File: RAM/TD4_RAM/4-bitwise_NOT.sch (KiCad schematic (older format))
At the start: 2 parts, among them U3 74HC04

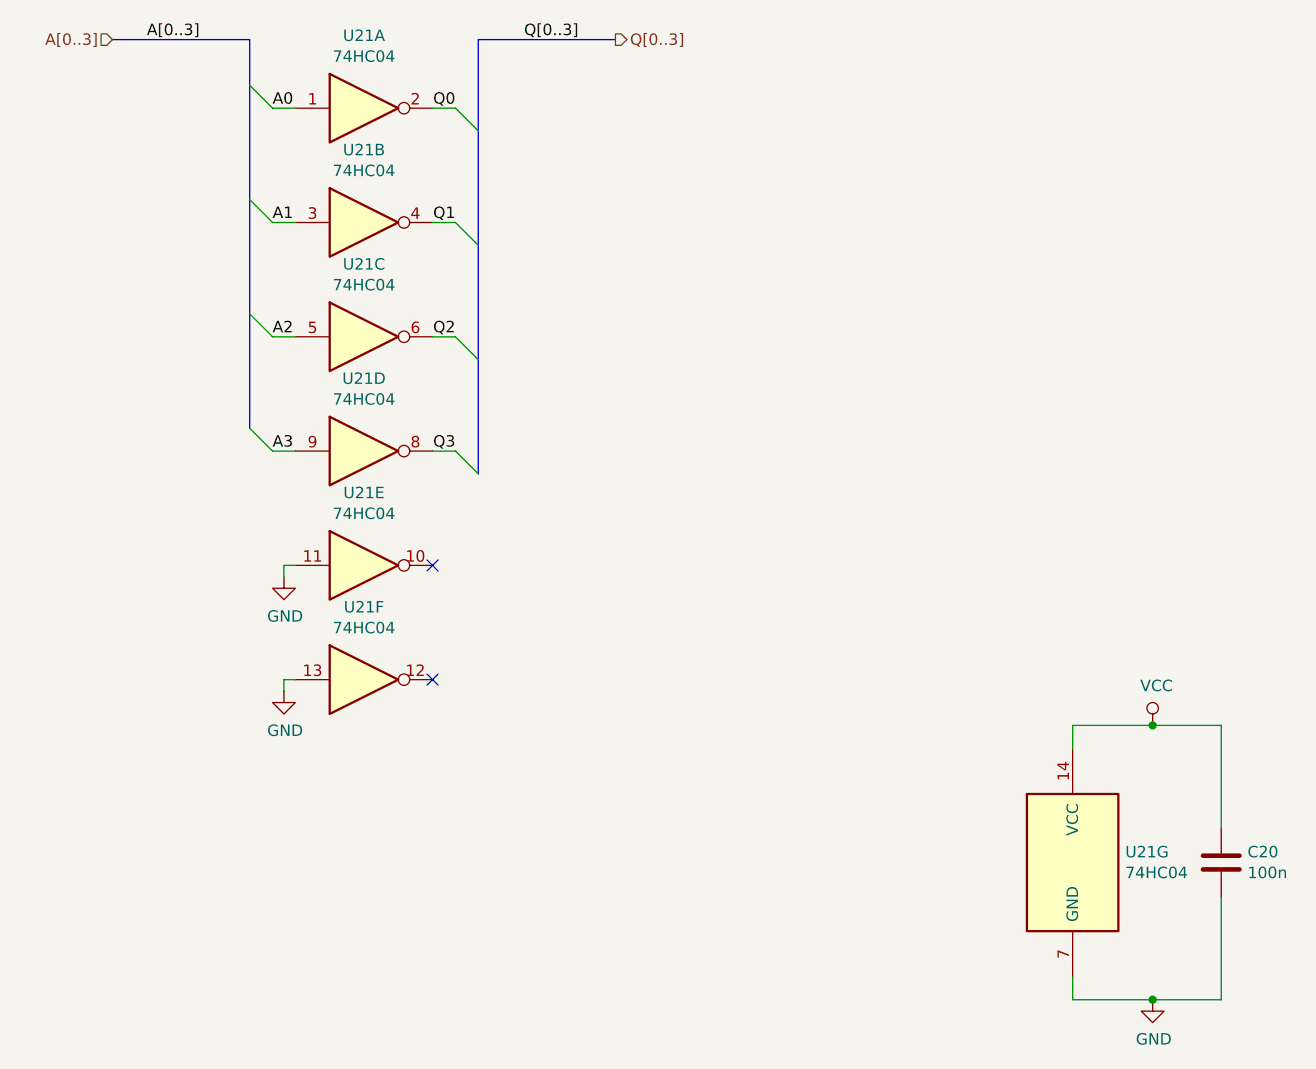
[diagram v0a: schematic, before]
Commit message: Added backplane connectors to all PCBs
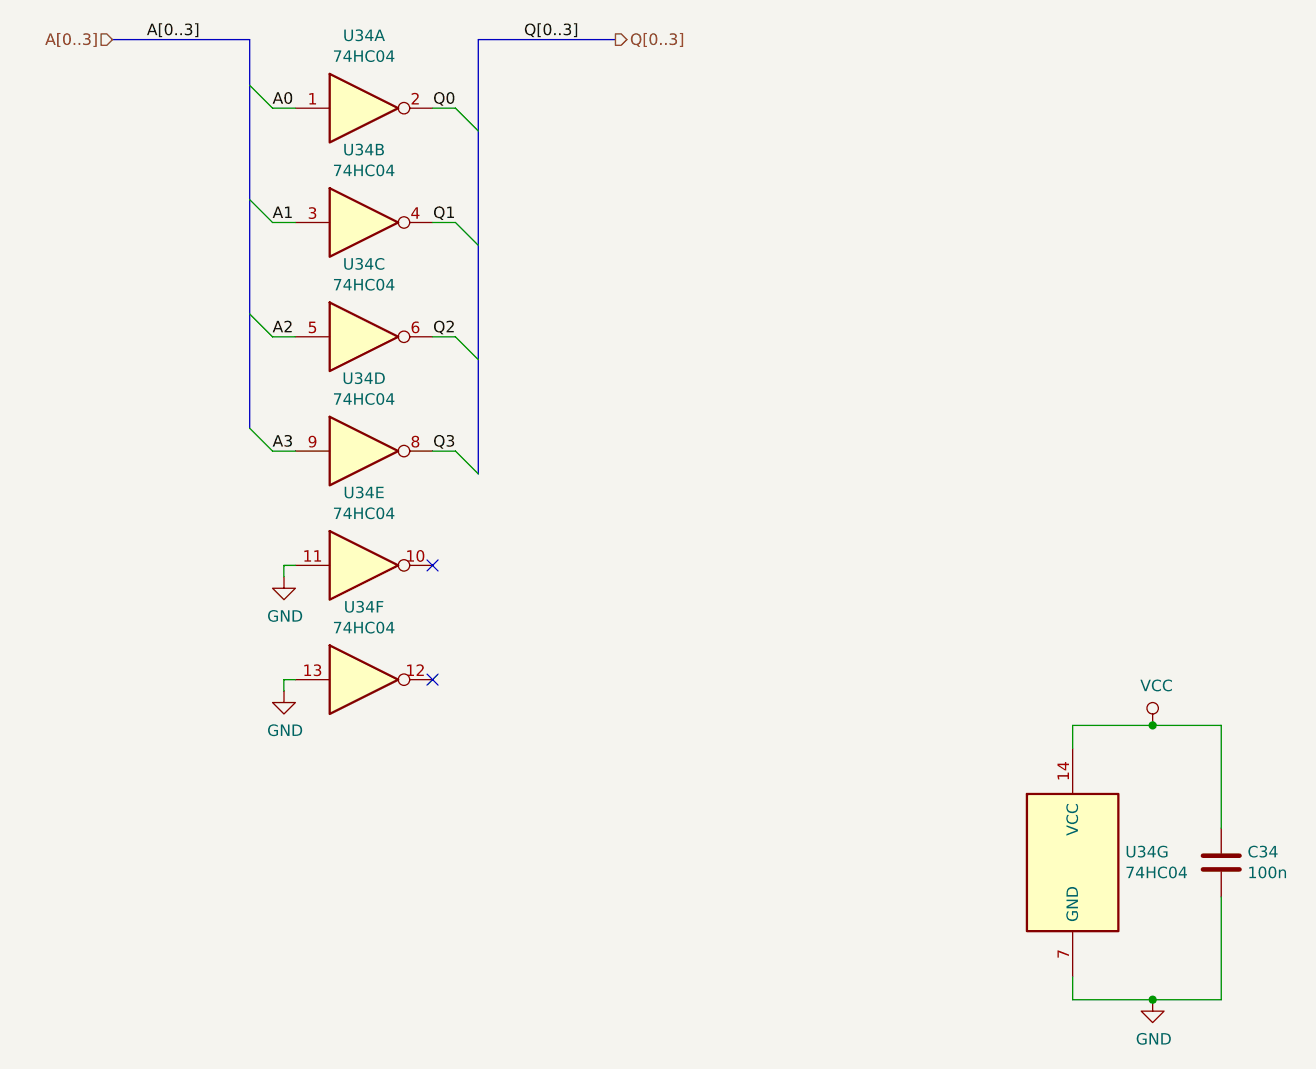
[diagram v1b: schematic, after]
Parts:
- C3: renamed from C2; footprint (none) -> Capacitor_SMD:C_0805_2012Metric
- U3: footprint (none) -> Package_SO:SOIC-14_3.9x8.7mm_P1.27mm

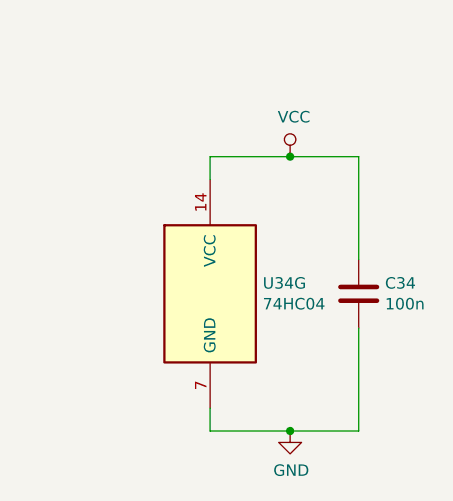
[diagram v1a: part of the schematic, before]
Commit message: Main RAM blocks routed
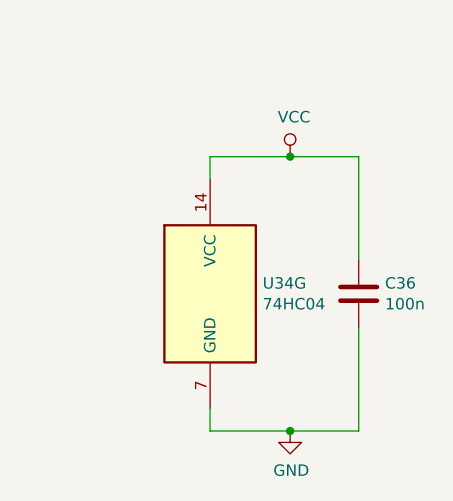
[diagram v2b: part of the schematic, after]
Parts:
- renumbered C3 to C5
